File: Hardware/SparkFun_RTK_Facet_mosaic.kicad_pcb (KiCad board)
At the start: 4 copper layers, 59.5 x 43 mm, 132 parts, among them J1 U.FL_SMD, J2 JST_2mm_LiPo, J3 Qwiic_RA, J5 Conn_01x12_FPC_0.5mm, J6 Conn_01x12_FPC_0.5mm, J7 Conn_01x12_FPC_0.5mm, Q1 MBT3904DW1, Q2 SIL2308, Q3 BSS138, U1 ESP32-WROVER-E-N16R8, U10 MCP73833_MSOP, U11 AP2112K-3.3, U12 STLQ015-3.3, U13 74HC4052D, U2 mosaic-X5, U3 CH340C, U4 MAX17048, U5 AP2112K-3.3, U9 USB251xB, Y1 24MHz

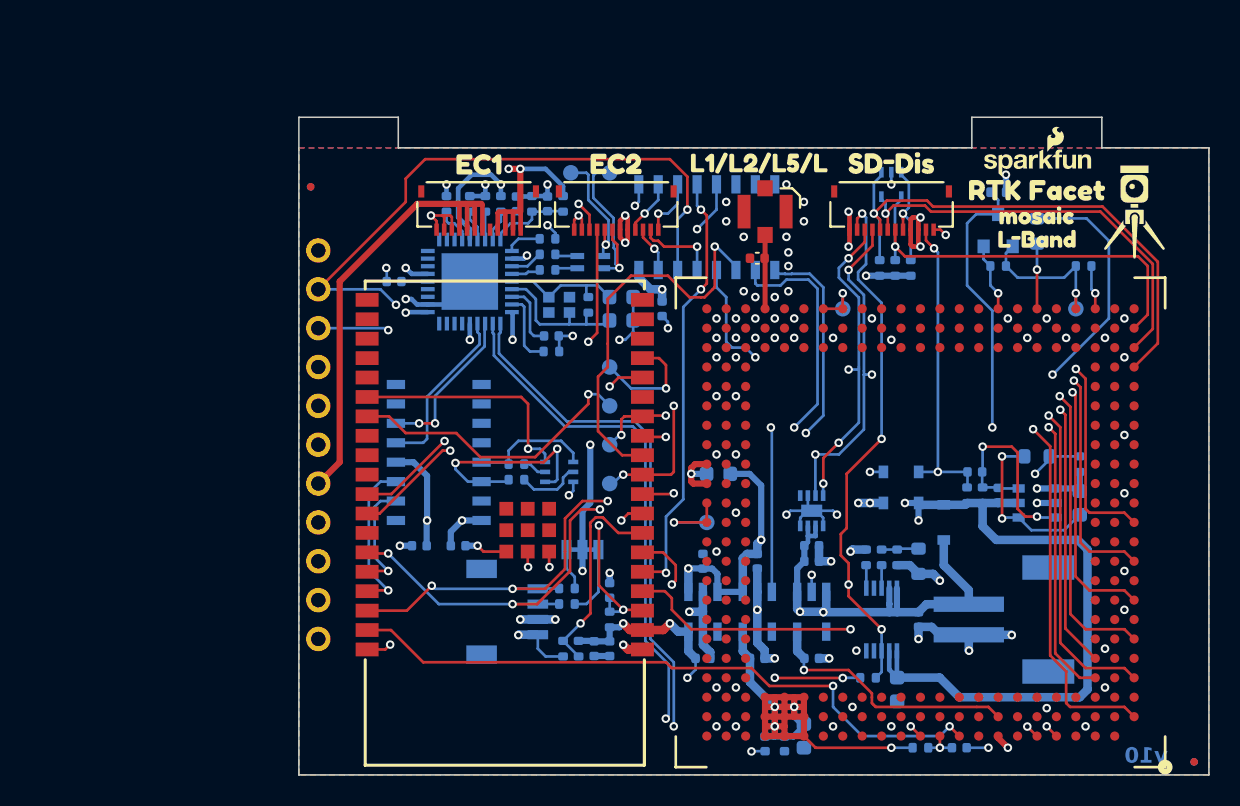
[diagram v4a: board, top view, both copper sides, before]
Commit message: With Buzzard text
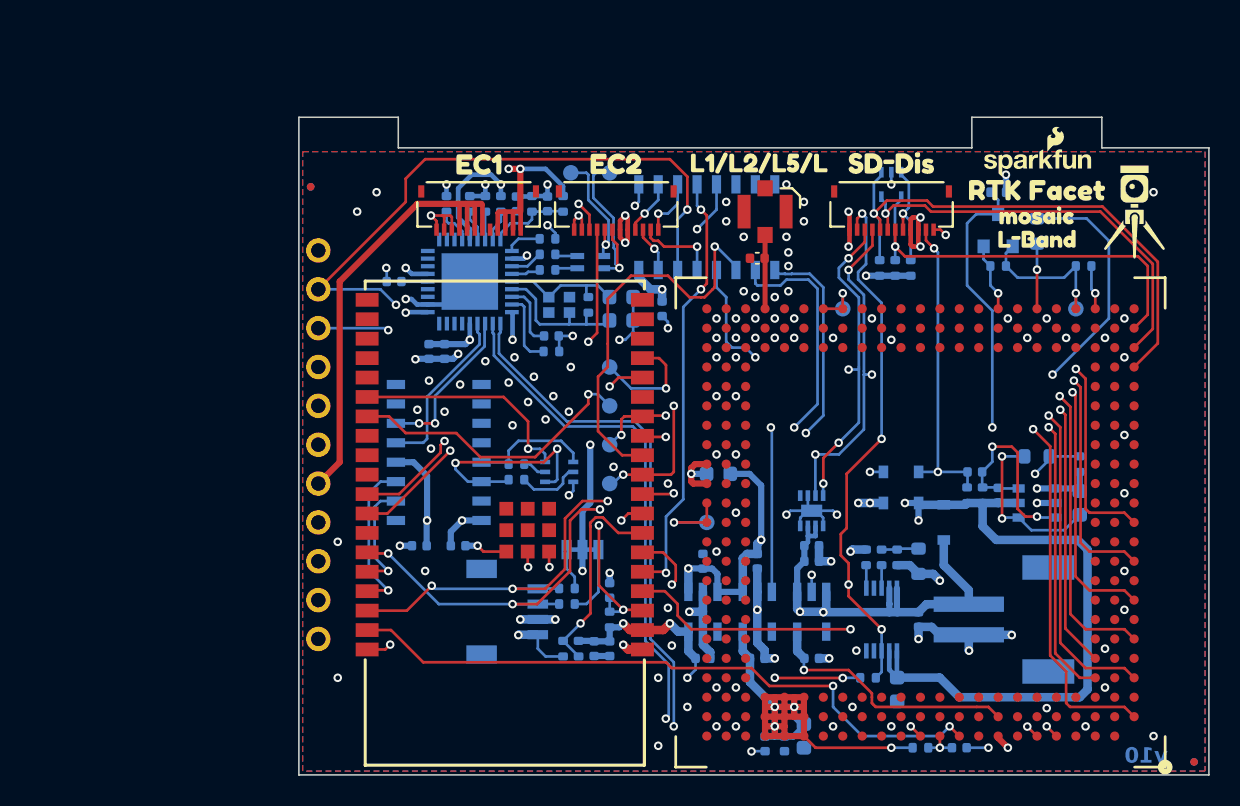
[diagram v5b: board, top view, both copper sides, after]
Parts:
- added C30: 0.1uF, SparkFun-Capacitor:C_0402_1005Metric, B.Cu at (111.1, 124.7)
- added C9: 2.2uF, SparkFun-Capacitor:C_0402_1005Metric, B.Cu at (110.1, 124.7)
- added kibuzzard-65A7F440: G***, kibuzzard-65A7F440, B.Cu at (105.4, 118.1)
- added kibuzzard-65A7F47C: G***, kibuzzard-65A7F47C, B.Cu at (105.2, 120.7)
- added kibuzzard-65A7F499: G***, kibuzzard-65A7F499, B.Cu at (105.3, 123.2)
- added kibuzzard-65A7F4A9: G***, kibuzzard-65A7F4A9, B.Cu at (105.8, 125.7)
- added kibuzzard-65A7F4BF: G***, kibuzzard-65A7F4BF, B.Cu at (105.2, 128.3)
- added kibuzzard-65A7F4D6: G***, kibuzzard-65A7F4D6, B.Cu at (105.4, 130.8)
- added kibuzzard-65A7F4E8: G***, kibuzzard-65A7F4E8, B.Cu at (105.4, 133.3)
- added kibuzzard-65A7F511: G***, kibuzzard-65A7F511, B.Cu at (105.3, 135.9)
- added kibuzzard-65A7F548: G***, kibuzzard-65A7F548, B.Cu at (105.8, 138.4)
- added kibuzzard-65A7F565: G***, kibuzzard-65A7F565, B.Cu at (105.3, 141.0)
- added kibuzzard-65A7F574: G***, kibuzzard-65A7F574, B.Cu at (105.4, 143.5)
- added kibuzzard-65A7F5A7: G***, kibuzzard-65A7F5A7, B.Cu at (124.0, 133.3)
- added kibuzzard-65A7F5BC: G***, kibuzzard-65A7F5BC, B.Cu at (123.8, 130.8)
- added kibuzzard-65A7F5CF: G***, kibuzzard-65A7F5CF, B.Cu at (124.1, 128.3)
- added kibuzzard-65A7F5E3: G***, kibuzzard-65A7F5E3, B.Cu at (124.0, 125.7)
- added kibuzzard-65A7F60E: G***, kibuzzard-65A7F60E, B.Cu at (130.3, 135.9)
- added kibuzzard-65A7F63F: G***, kibuzzard-65A7F63F, B.Cu at (135.1, 121.9)
- added kibuzzard-65A7F686: G***, kibuzzard-65A7F686, B.Cu at (118.0, 112.3)
- added kibuzzard-65A7F697: G***, kibuzzard-65A7F697, B.Cu at (123.2, 112.3)
- added kibuzzard-65A7F771: G***, kibuzzard-65A7F771, B.Cu at (154.4, 121.9)
- added kibuzzard-65A7F7BA: G***, kibuzzard-65A7F7BA, B.Cu at (145.8, 139.8)
- added kibuzzard-65A7F7EA: G***, kibuzzard-65A7F7EA, B.Cu at (145.8, 144.7)
- added kibuzzard-65A7F891: G***, kibuzzard-65A7F891, B.Cu at (123.3, 137.7)
- TR1: value RFCMF1220100M4T -> Val**
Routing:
- net GND: track 82.7 -> 85.7 mm, vias 95 -> 126
- net 3.3V: track 117.0 -> 119.8 mm
- net ESP0/BOOT: track 15.4 -> 14.8 mm

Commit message: Do over with RSP32 Pico Mini - routed
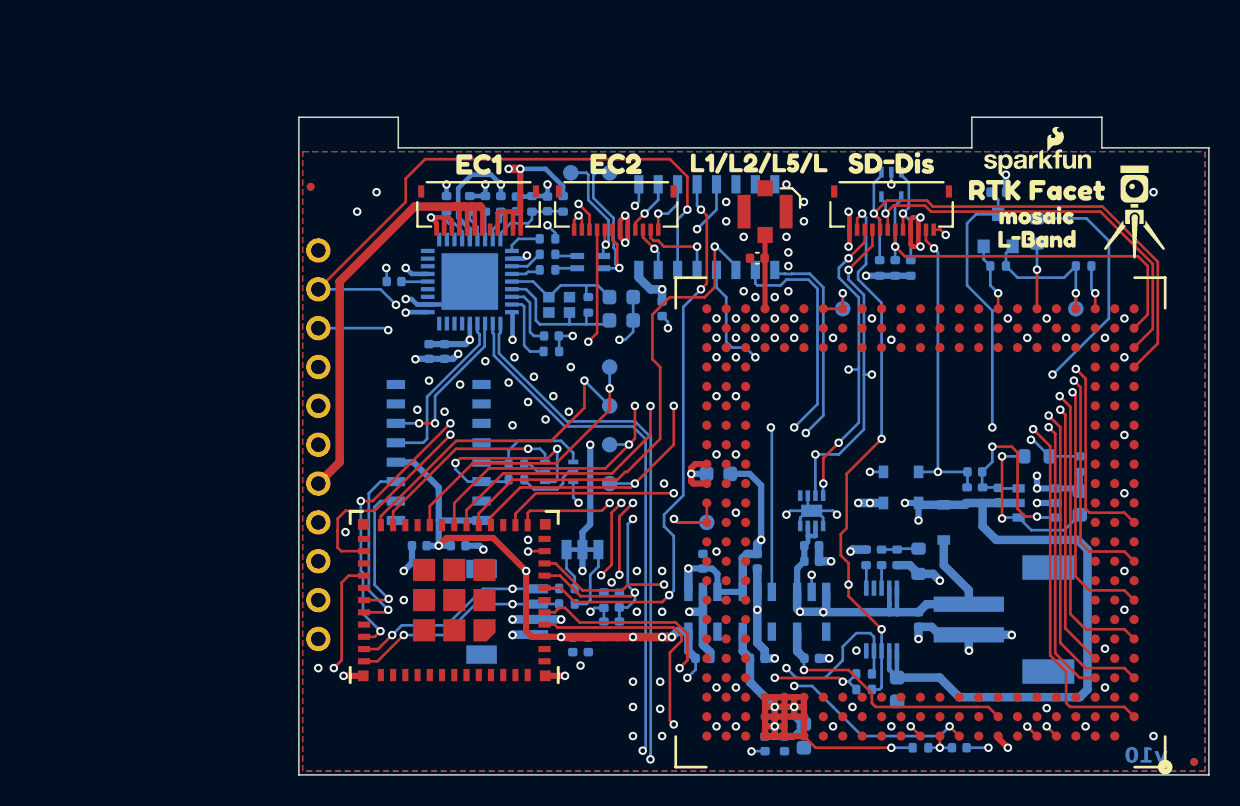
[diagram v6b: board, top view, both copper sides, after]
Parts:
- added R9: 10k, SparkFun-Resistor:R_0402_1005Metric, B.Cu at (138.6, 145.8)
- TR1: value Val** -> RFCMF1220100M4T
- U1: value ESP32-WROVER-E-N16R8 -> ESP32-PICO-V3-02; footprint SparkFun-RF:ESP32-WROVER-E-IE -> SparkFun-RF:ESP32-PICO-MINI
- moved U1 5.64 mm to (111.8, 141.0), turned to 180 degrees
- moved R8 4.15 mm to (121.5, 141.0), turned to 90 degrees
- moved R7 2.08 mm to (121.5, 142.9), turned to 90 degrees
- moved C2 1.42 mm to (120.5, 143.9)
- moved C1 1.42 mm to (119.5, 143.9)
- moved R1 0.90 mm to (122.6, 142.9)
- moved C8 0.90 mm to (122.6, 141.0)
- moved R10 0.80 mm to (138.6, 146.8)
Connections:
- U1 pad 10: ESP25/MRX4 -> ESP35/DeviceSense
- U1 pad 11: ESP26/DAC2 -> GND
- U1 pad 12: ESP27/PeripheralPower -> ESP32/PowerControl
- U1 pad 13: ESP14/MRX1 -> ESP33/FastOff
- U1 pad 14: unconnected-(U1-IOA12-Pad14) -> GND
- U1 pad 15: GND -> ESP25/MRX4
- U1 pad 16: ESP13/MTX1 -> ESP26/DAC2
- U1 pad 17: unconnected-(U1-NC-Pad17) -> ESP27/PeripheralPower
- U1 pad 18: unconnected-(U1-NC-Pad18) -> ESP14/MRX1
- U1 pad 2: 3.3V -> GND
- U1 pad 20: unconnected-(U1-NC-Pad20) -> ESP13/MTX1
- U1 pad 23: unconnected-(U1-IOA15-Pad23) -> ESP0/BOOT
- U1 pad 24: unconnected-(U1-IOA2-Pad24) -> ESP4/MTX4
- U1 pad 25: ESP0/BOOT -> unconnected-(U1-NC-Pad25)
- U1 pad 26: ESP4/MTX4 -> ESP20/MUXB
- U1 pad 28: unconnected-(U1-NC-Pad28) -> ESP8/MOnOff
- U1 pad 3: ESP~{RST} -> 3.3V
- U1 pad 30: ESP18/MUXA -> ESP3/CH340-TX
- U1 pad 31: ESP19/MUXB -> ESP1/CH340-RX
- U1 pad 33: ESP21/SDA -> ESP19/MUXA
- U1 pad 34: ESP3/CH340-TX -> ESP22/SCL
- U1 pad 35: ESP1/CH340-RX -> ESP21/SDA
- U1 pad 36: ESP22/SCL -> GND
- U1 pad 37: ESP23/MOnOff -> GND
- U1 pad 5: ESP39/ADC39 -> ESP37/CHG_STAT2
- U1 pad 6: ESP34/CHG_LED -> unconnected-(U1-IA38-Pad6)
- U1 pad 7: ESP35/DeviceSense -> ESP39/ADC39
- U1 pad 8: ESP32/PowerControl -> ESP~{RST}
- U1 pad 9: ESP33/FastOff -> ESP34/CHG_LED
- U10 pad 4: unconnected-(U10-STAT2-Pad4) -> ESP37/CHG_STAT2
- U13 pad 10: ESP18/MUXA -> ESP19/MUXA
- U13 pad 9: ESP19/MUXB -> ESP20/MUXB
- U2 pad A10: ESP23/MOnOff -> ESP8/MOnOff
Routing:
- net ESP19/MUXA: track 0.00 -> 57.5 mm, vias 0 -> 4
- net ESP8/MOnOff: track 0.00 -> 52.3 mm, vias 0 -> 3
- net ESP20/MUXB: track 0.00 -> 51.8 mm, vias 0 -> 2
- net ESP18/MUXA: track 46.0 -> 0.00 mm, vias 2 -> 0
- net ESP19/MUXB: track 45.1 -> 0.00 mm, vias 2 -> 0
- net ESP23/MOnOff: track 42.9 -> 0.00 mm, vias 2 -> 0
- net ESP37/CHG_STAT2: track 0.00 -> 29.9 mm, vias 0 -> 2
- net ESP27/PeripheralPower: track 19.5 -> 36.3 mm
- net ESP14/MRX1: track 53.3 -> 69.4 mm
- net ESP13/MTX1: track 54.5 -> 69.1 mm
- net GND: track 85.7 -> 75.8 mm, vias 126 -> 128
- net ESP25/MRX4: track 52.5 -> 62.3 mm
- net ESP33/FastOff: track 35.9 -> 45.6 mm
- net ESP39/ADC39: track 28.3 -> 37.4 mm
- net ESP36/MRDY: track 24.1 -> 32.5 mm
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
